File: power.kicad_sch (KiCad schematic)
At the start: 14 parts, among them U3 TPS7A2050PDQNR, U4 TPS61040DBV

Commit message: rough blocking out the pcb
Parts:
- added TP2, TP3: TestPoint, TestPoint:TestPoint_THTPad_1.5x1.5mm_Drill0.7mm, symbol Connector:TestPoint
- JP3: footprint (none) -> Jumper:SolderJumper-2_P1.3mm_Open_TrianglePad1.0x1.5mm
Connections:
- net VBOOST: now also TP2.1
- net VHAPPY: now also TP3.1
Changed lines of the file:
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@@
+	)
+	(junction
+		(at 139.7 50.8)
+		(diameter 0)
+		(color 0 0 0 0)
 	)
 	(junction
@@
 	(wire
 		(pts
-			(xy 134.62 50.8) (xy 146.05 50.8)
+			(xy 134.62 50.8) (xy 139.7 50.8)
 		)
 		(stroke
@@
 		(pts
 			(xy 97.79 60.96) (xy 91.44 60.96)
+		)
+		(stroke
+			(width 0)
+			(type default)
+		)
+	)
+	(wire
+		(pts
+			(xy 139.7 50.8) (xy 146.05 50.8)
 		)
 		(stroke
@@
 			)
 		)
-		(property "Footprint" ""
+		(property "Footprint" "Jumper:SolderJumper-2_P1.3mm_Open_TrianglePad1.0x1.5mm"
 			(at 114.3 165.1 0)
 			(effects
@@
 	)
 	(symbol
+		(lib_id "Connector:TestPoint")
+		(at 139.7 50.8 0)
+		(unit 1)
+		(exclude_from_sim no)
+		(in_bom yes)
+		(on_board yes)
+		(dnp no)
+		(fields_autoplaced yes)
+		(property "Reference" "TP2"
+			(at 142.24 46.2279 0)
+			(effects
+				(font
+					(size 1.27 1.27)
+				)
+				(justify left)
+			)
+		)
+		(property "Value" "TestPoint"
+			(at 142.24 48.7679 0)
+			(effects
+				(font
+					(size 1.27 1.27)
+				)
+				(justify left)
+			)
+		)
+		(property "Footprint" "TestPoint:TestPoint_THTPad_1.5x1.5mm_Drill0.7mm"
+			(at 144.78 50.8 0)
+			(effects
+				(font
+					(size 1.27 1.27)
+				)
+				(hide yes)
+			)
+		)
+		(property "Datasheet" "~"
+			(at 144.78 50.8 0)
+			(effects
+				(font
+					(size 1.27 1.27)
+				)
+				(hide yes)
+			)
+		)
+		(property "Description" "test point"
+			(at 139.7 50.8 0)
+			(effects
+				(font
+					(size 1.27 1.27)
+				)
+				(hide yes)
+			)
+		)
+		(pin "1"
+		)
+		(instances
+			(project ""
+				(path "/e63e39d7-6ac0-4ffd-8aa3-1841a4541b55/fdbfdc15-850a-4ffd-858c-b9b4d340c2f9"
+					(reference "TP2")
+					(unit 1)
+				)
+			)
+		)
+	)
+	(symbol
 		(lib_id "Regulator_Switching:TPS61040DBV")
 		(at 105.41 63.5 0)
@@
 					(unit 1)
 				)
+			)
+		)
+	)
+	(symbol
+		(lib_id "Connector:TestPoint")
+		(at 139.7 101.6 0)
+		(unit 1)
+		(exclude_from_sim no)
+		(in_bom yes)
+		(on_board yes)
+		(dnp no)
+		(fields_autoplaced yes)
+		(property "Reference" "TP3"
+			(at 142.24 97.0279 0)
+			(effects
+				(font
+					(size 1.27 1.27)
+				)
+				(justify left)
+			)
+		)
+		(property "Value" "TestPoint"
+			(at 142.24 99.5679 0)
+			(effects
+				(font
+					(size 1.27 1.27)
+				)
+				(justify left)
+			)
+		)
+		(property "Footprint" "TestPoint:TestPoint_THTPad_1.5x1.5mm_Drill0.7mm"
+			(at 144.78 101.6 0)
+			(effects
+				(font
+					(size 1.27 1.27)
+				)
+				(hide yes)
+			)
+		)
+		(property "Datasheet" "~"
+			(at 144.78 101.6 0)
+			(effects
+				(font
+					(size 1.27 1.27)
+				)
+				(hide yes)
+			)
+		)
+		(property "Description" "test point"
+			(at 139.7 101.6 0)
+			(effects
+				(font
+					(size 1.27 1.27)
+				)
+				(hide yes)
+			)
+		)
+		(pin "1"
+		)
+		(instances
+			(project "pi-hat-hx711_r1"
+				(path "/e63e39d7-6ac0-4ffd-8aa3-1841a4541b55/fdbfdc15-850a-4ffd-858c-b9b4d340c2f9"
+					(reference "TP3")
+					(unit 1)
+				)

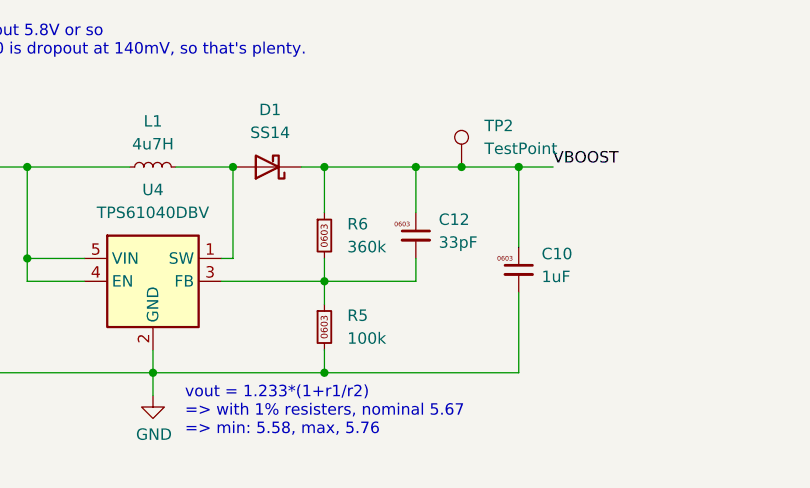
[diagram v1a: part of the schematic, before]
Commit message: better parts, start pushing layout blocks
SMA is dumb, way too big
the swpa3030 was... unnecessarily small. we're trying to be super chill
power here, don't push it hot.  (Still, 1A was.. really, more than
enough? but 1A is a 40C rise, so.. let's just have less....)
use more caps too. why the fuck not. more filtering, more happy.

holy fuck though, kicad on wayland is giving me the shits!
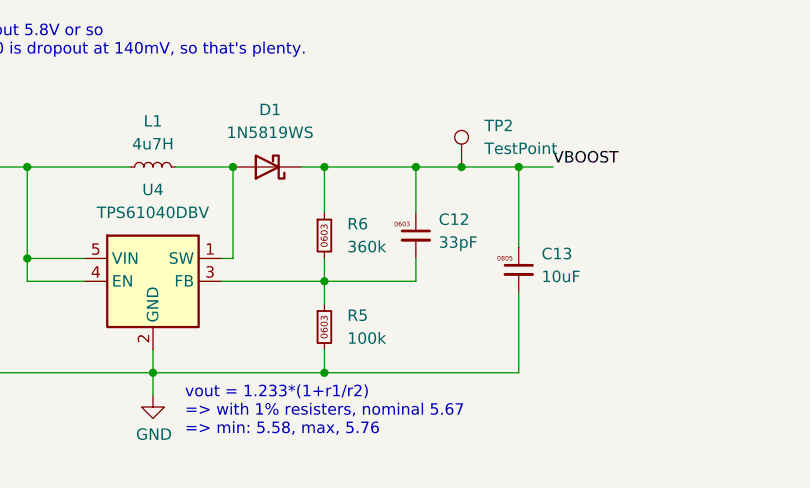
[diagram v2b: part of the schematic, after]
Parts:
- removed C10: 1uF, Capacitor_SMD:C_0603_1608Metric, symbol karl-marel-atomics:KC0603_1uF
- removed D1: SS14, Diode_SMD:D_SMA, symbol Diode:SS14
- added C13: 10uF, Capacitor_SMD:C_0805_2012Metric, symbol karl-marel-atomics:KC0805_10uF_25V
- added D1: 1N5819WS, Diode_SMD:D_SOD-323, symbol Diode:1N5819WS
- C11, C12, C6, C7, C8, R5, R6, R7: jlcbasic (none) -> basic
- L1: footprint Inductor_SMD:L_Sunlord_SWPA3015S -> Inductor_SMD:L_Changjiang_FNR4030S; LCSC Part # C19398 -> C167874; MPN SWPA3015S4R7MT -> FNR4030S4R7MT; jlcbasic (none) -> 0
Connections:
- net GND: now also C13.2
- net VBOOST: now also C13.1, D1.1 (K)
- net at L1.2, U4.1 (SW): now also D1.2 (A)

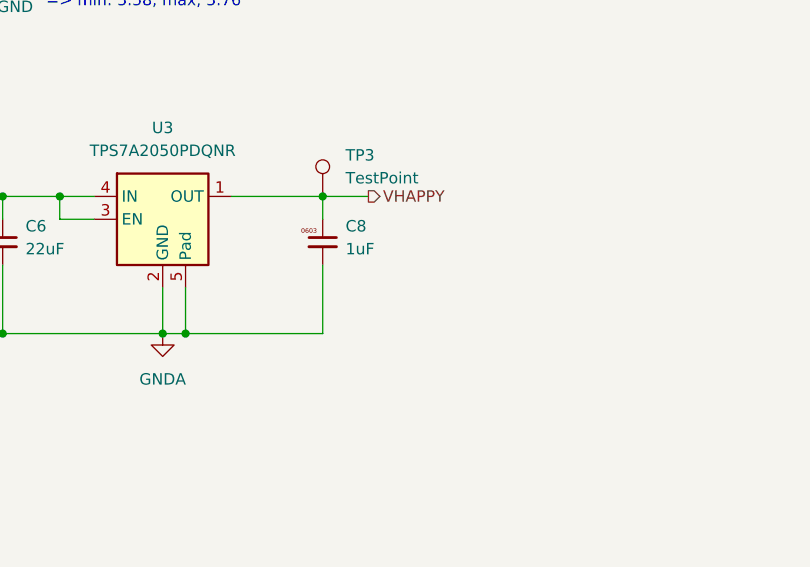
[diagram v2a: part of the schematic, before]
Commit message: add second channel input
switch to vertical connectors, so no concerns abotu edge space.
Allows offering the second channel, even though it's probably useless,
but it sets us up with a style we might be ok with for subsequent
boards.
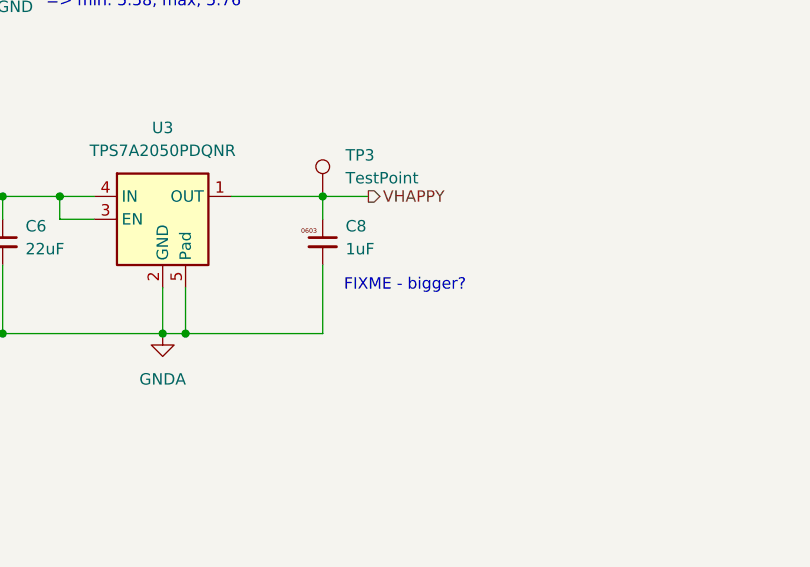
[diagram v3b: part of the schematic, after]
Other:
- note added: "FIXME - bigger?"
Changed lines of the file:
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@@
+		)
+	)
+	(text "FIXME - bigger?"
+		(exclude_from_sim no)
+		(at 148.844 111.506 0)
+		(effects
+			(font
+				(size 1.27 1.27)
+			)
 		)
 	)

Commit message: pushing blocks
roughyl how we want it?
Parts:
- added TP4: TestPoint, TestPoint:TestPoint_THTPad_1.5x1.5mm_Drill0.7mm, symbol Connector:TestPoint
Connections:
- net GNDA: now also TP4.1
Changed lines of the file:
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@@
+	)
+	(symbol
+		(lib_id "power:GNDA")
+		(at 139.7 124.46 0)
+		(unit 1)
+		(exclude_from_sim no)
+		(in_bom yes)
+		(on_board yes)
+		(dnp no)
+		(fields_autoplaced yes)
+		(property "Reference" "#PWR05"
+			(at 139.7 130.81 0)
+			(effects
+				(font
+					(size 1.27 1.27)
+				)
+				(hide yes)
+			)
+		)
+		(property "Value" "GNDA"
+			(at 139.7 129.54 0)
+			(effects
+				(font
+					(size 1.27 1.27)
+				)
+			)
+		)
+		(property "Footprint" ""
+			(at 139.7 124.46 0)
+			(effects
+				(font
+					(size 1.27 1.27)
+				)
+				(hide yes)
+			)
+		)
+		(property "Datasheet" ""
+			(at 139.7 124.46 0)
+			(effects
+				(font
+					(size 1.27 1.27)
+				)
+				(hide yes)
+			)
+		)
+		(property "Description" "Power symbol creates a global label with name \"GNDA\" , analog ground"
+			(at 139.7 124.46 0)
+			(effects
+				(font
+					(size 1.27 1.27)
+				)
+				(hide yes)
+			)
+		)
+		(pin "1"
+		)
+		(instances
+			(project "pi-hat-hx711_r1"
+				(path "/e63e39d7-6ac0-4ffd-8aa3-1841a4541b55/fdbfdc15-850a-4ffd-858c-b9b4d340c2f9"
+					(reference "#PWR05")
+					(unit 1)
+				)
+			)
+		)
 	)
 	(symbol
@@
 					(unit 1)
 				)
+			)
+		)
+	)
+	(symbol
+		(lib_id "Connector:TestPoint")
+		(at 139.7 124.46 0)
+		(unit 1)
+		(exclude_from_sim no)
+		(in_bom yes)
+		(on_board yes)
+		(dnp no)
+		(fields_autoplaced yes)
+		(property "Reference" "TP4"
+			(at 142.24 119.8879 0)
+			(effects
+				(font
+					(size 1.27 1.27)
+				)
+				(justify left)
+			)
+		)
+		(property "Value" "TestPoint"
+			(at 142.24 122.4279 0)
+			(effects
+				(font
+					(size 1.27 1.27)
+				)
+				(justify left)
+			)
+		)
+		(property "Footprint" "TestPoint:TestPoint_THTPad_1.5x1.5mm_Drill0.7mm"
+			(at 144.78 124.46 0)
+			(effects
+				(font
+					(size 1.27 1.27)
+				)
+				(hide yes)
+			)
+		)
+		(property "Datasheet" "~"
+			(at 144.78 124.46 0)
+			(effects
+				(font
+					(size 1.27 1.27)
+				)
+				(hide yes)
+			)
+		)
+		(property "Description" "test point"
+			(at 139.7 124.46 0)
+			(effects
+				(font
+					(size 1.27 1.27)
+				)
+				(hide yes)
+			)
+		)
+		(pin "1"
+		)
+		(instances
+			(project "pi-hat-hx711_r1"
+				(path "/e63e39d7-6ac0-4ffd-8aa3-1841a4541b55/fdbfdc15-850a-4ffd-858c-b9b4d340c2f9"
+					(reference "TP4")
+					(unit 1)
+				)

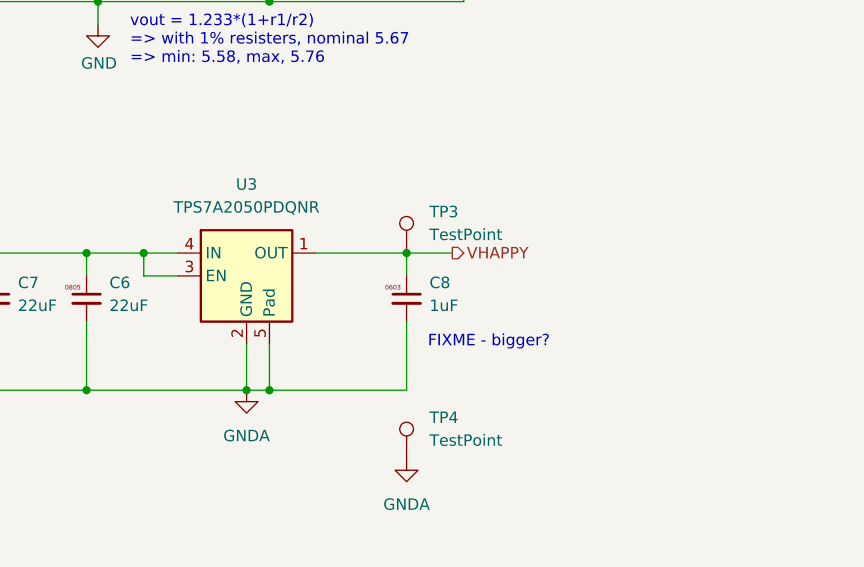
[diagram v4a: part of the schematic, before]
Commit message: chunk out routing
looks okish?

switched x2son for plain sot235, it's better stocked at jlc anyway, and
easier to probe and work with.
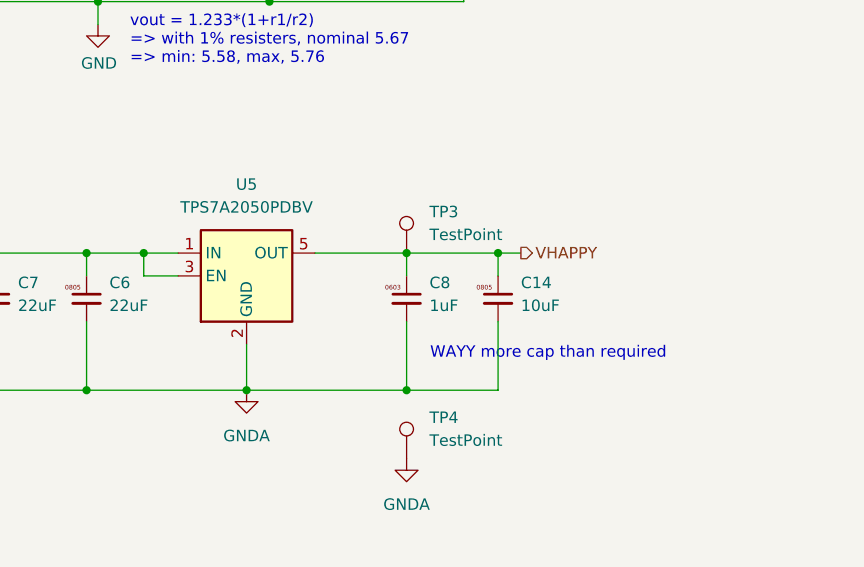
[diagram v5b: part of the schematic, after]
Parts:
- removed U3: TPS7A2050PDQNR, Package_SON:Texas_X2SON-4_1x1mm_P0.65mm, symbol Regulator_Linear:TPS7A20xxxDQN
- added C14: 10uF, Capacitor_SMD:C_0805_2012Metric, symbol karl-marel-atomics:KC0805_10uF_25V
- added U5: TPS7A2050PDBV, Package_TO_SOT_SMD:SOT-23-5, symbol Regulator_Linear:TPS7A0515PDBV
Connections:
- net GNDA: now also C14.2, U5.2 (GND)
- net VHAPPY: now also C14.1, U5.5 (OUT)
- net at C6.1, C7.1, R7.2: now also U5.1 (IN), U5.3 (EN)
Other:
- note added: "WAYY more cap than required"
- note removed: "FIXME - bigger?"
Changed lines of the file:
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@@
-		)
-	)
-	(text "FIXME - bigger?"
-		(exclude_from_sim no)
-		(at 148.844 111.506 0)
-		(effects
-			(font
-				(size 1.27 1.27)
-			)
 		)
 	)
@@
 		)
 	)
-	(junction
-		(at 124.46 116.84)
-		(diameter 0)
-		(color 0 0 0 0)
+	(text "WAYY more cap than required"
+		(exclude_from_sim no)
+		(at 155.448 112.776 0)
+		(effects
+			(font
+				(size 1.27 1.27)
+			)
+		)
 	)
 	(junction
@@
 	)
 	(junction
+		(at 149.86 101.6)
+		(diameter 0)
+		(color 0 0 0 0)
+	)
+	(junction
 		(at 80.01 50.8)
 		(diameter 0)
@@
 	)
 	(junction
+		(at 139.7 116.84)
+		(diameter 0)
+		(color 0 0 0 0)
+	)
+	(junction
 		(at 146.05 50.8)
 		(diameter 0)
@@
 	(wire
 		(pts
-			(xy 124.46 111.76) (xy 124.46 116.84)
-		)
-		(stroke
-			(width 0)
-			(type default)
-		)
-	)
-	(wire
-		(pts
 			(xy 76.2 50.8) (xy 80.01 50.8)
 		)
@@
 	(wire
 		(pts
+			(xy 149.86 101.6) (xy 149.86 104.14)
+		)
+		(stroke
+			(width 0)
+			(type default)
+		)
+	)
+	(wire
+		(pts
 			(xy 91.44 50.8) (xy 102.87 50.8)
 		)
@@
 	(wire
 		(pts
-			(xy 124.46 116.84) (xy 121.92 116.84)
+			(xy 121.92 116.84) (xy 139.7 116.84)
 		)
 		(stroke
@@
 	(wire
 		(pts
+			(xy 149.86 116.84) (xy 139.7 116.84)
+		)
+		(stroke
+			(width 0)
+			(type default)
+		)
+	)
+	(wire
+		(pts
 			(xy 104.14 101.6) (xy 110.49 101.6)
 		)
@@
 	(wire
 		(pts
+			(xy 149.86 109.22) (xy 149.86 116.84)
+		)
+		(stroke
+			(width 0)
+			(type default)
+		)
+	)
+	(wire
+		(pts
 			(xy 104.14 116.84) (xy 121.92 116.84)
 		)
@@
 	(wire
 		(pts
-			(xy 139.7 116.84) (xy 124.46 116.84)
-		)
-		(stroke
-			(width 0)
-			(type default)
-		)
-	)
-	(wire
-		(pts
 			(xy 93.98 101.6) (xy 93.98 104.14)
 		)
@@
 	(wire
 		(pts
-			(xy 139.7 101.6) (xy 144.78 101.6)
+			(xy 139.7 101.6) (xy 149.86 101.6)
 		)
 		(stroke
@@
 		(pts
 			(xy 124.46 60.96) (xy 124.46 63.5)
+		)
+		(stroke
+			(width 0)
+			(type default)
+		)
+	)
+	(wire
+		(pts
+			(xy 149.86 101.6) (xy 152.4 101.6)
 		)
 		(stroke
@@
 	(hierarchical_label "VHAPPY"
 		(shape output)
-		(at 144.78 101.6 0)
+		(at 152.4 101.6 0)
 		(effects
 			(font
@@
 	)
 	(symbol
+		(lib_id "karl-marel-atomics:KC0805_10uF_25V")
+		(at 149.86 106.68 0)
+		(unit 1)
+		(exclude_from_sim no)
+		(in_bom yes)
+		(on_board yes)
+		(dnp no)
+		(fields_autoplaced yes)
+		(property "Reference" "C14"
+			(at 152.4 104.9071 0)
+			(effects
+				(font
+					(size 1.27 1.27)
+				)
+				(justify left)
+			)
+		)
+		(property "Value" "10uF"
+			(at 152.4 107.4471 0)
+			(effects
+				(font
+					(size 1.27 1.27)
+				)
+				(justify left)
+			)
+		)
+		(property "Footprint" "Capacitor_SMD:C_0805_2012Metric"
+			(at 149.352 110.49 0)
+			(effects
+				(font
+					(size 1.27 1.27)
+				)
+				(hide yes)
+			)
+		)
+		(property "Datasheet" "~"
+			(at 149.86 106.68 0)
+			(effects
+				(font
+					(size 1.27 1.27)
+				)
+				(hide yes)
+			)
+		)
+		(property "Description" "25V, X5R"
+			(at 149.86 110.49 0)
+			(effects
+				(font
+					(size 1.27 1.27)
+				)
+				(hide yes)
+			)
+		)
+		(property "MPN" "CL21A106KAYNNNE"
+			(at 149.606 110.49 0)
+			(effects
+				(font
+					(size 1.27 1.27)
+				)
+				(hide yes)
+			)
+		)
+		(property "LCSC Part #" "C15850"
+			(at 149.86 110.49 0)
+			(effects
+				(font
+					(size 1.27 1.27)
+				)
+				(hide yes)
+			)
+		)
+		(property "jlcbasic" "basic"
+			(at 149.86 106.68 0)
+			(effects
+				(font
+					(size 1.27 1.27)
+				)
+				(hide yes)
+			)
+		)
+		(pin "1"
+		)
+		(pin "2"
+		)
+		(instances
+			(project "pi-hat-hx711_r1"
+				(path "/e63e39d7-6ac0-4ffd-8aa3-1841a4541b55/fdbfdc15-850a-4ffd-858c-b9b4d340c2f9"
+					(reference "C14")
+					(unit 1)
+				)
+			)
+		)
+	)
+	(symbol
 		(lib_id "karl-marel-atomics:KC0805_22uF_25V")
 		(at 80.01 60.96 0)
@@
 	)
 	(symbol
-		(lib_id "Regulator_Linear:TPS7A20xxxDQN")
-		(at 121.92 104.14 0)
-		(unit 1)
-		(exclude_from_sim no)
-		(in_bom yes)
-		(on_board yes)
-		(dnp no)
-		(fields_autoplaced yes)
-		(property "Reference" "U3"
-			(at 121.92 93.98 0)
-			(effects
-				(font
-					(size 1.27 1.27)
-				)
-			)
-		)
-		(property "Value" "TPS7A2050PDQNR"
-			(at 121.92 96.52 0)
-			(effects
-				(font
-					(size 1.27 1.27)
-				)
-			)
-		)
-		(property "Footprint" "Package_SON:Texas_X2SON-4_1x1mm_P0.65mm"
-			(at 121.92 95.25 0)
-			(effects
-				(font
-					(size 1.27 1.27)
-				)
-				(hide yes)
-			)
-		)
-		(property "Datasheet" "https://www.ti.com/lit/ds/symlink/tps7a20.pdf"
-			(at 121.92 91.44 0)
-			(effects
-				(font
-					(size 1.27 1.27)
-				)
-				(hide yes)
-			)
-		)
-		(property "Description" "300 mA Low Dropout Voltage Regulator, Fixed Output, 1.6..6.0Vin, Low-Noise (7μV RMS), 6.5μA IQ LDO, X2SON-5"
-			(at 121.92 104.14 0)
-			(effects
-				(font
-					(size 1.27 1.27)
-				)
-				(hide yes)
-			)
-		)
-		(property "LCSC Part #" "C2866499"
-			(at 121.92 104.14 0)
-			(effects
-				(font
-					(size 1.27 1.27)
-				)
-				(hide yes)
-			)
-		)
-		(property "MPN" "TPS7A2050PDQNR"
-			(at 121.92 104.14 0)
-			(effects
-				(font
-					(size 1.27 1.27)
-				)
-				(hide yes)
-			)
-		)
-		(property "jlcbasic" "0"
-			(at 121.92 104.14 0)
-			(effects
-				(font
-					(size 1.27 1.27)
-				)
-				(hide yes)
-			)
-		)
-		(pin "1"
-		)
-		(pin "5"
-		)
-		(pin "4"
-		)
-		(pin "3"
-		)
-		(pin "2"
-		)
-		(instances
-			(project "pi-hat-hx711_r1"
-				(path "/e63e39d7-6ac0-4ffd-8aa3-1841a4541b55/fdbfdc15-850a-4ffd-858c-b9b4d340c2f9"
-					(reference "U3")
-					(unit 1)
-				)
-			)
-		)
-	)
-	(symbol
 		(lib_id "Diode:1N5819WS")
 		(at 118.11 50.8 180)
@@
 					(unit 1)
 				)
+			)
+		)
+	)
+	(symbol
+		(lib_id "Regulator_Linear:TPS7A0515PDBV")
+		(at 121.92 104.14 0)
+		(unit 1)
+		(exclude_from_sim no)
+		(in_bom yes)
+		(on_board yes)
+		(dnp no)
+		(fields_autoplaced yes)
+		(property "Reference" "U5"
+			(at 121.92 93.98 0)
+			(effects
+				(font
+					(size 1.27 1.27)
+				)
+			)
+		)
+		(property "Value" "TPS7A2050PDBV"
+			(at 121.92 96.52 0)
+			(effects
+				(font
+					(size 1.27 1.27)
+				)
+			)
+		)
+		(property "Footprint" "Package_TO_SOT_SMD:SOT-23-5"
+			(at 121.92 95.25 0)
+			(effects
+				(font
+					(size 1.27 1.27)
+				)
+				(hide yes)
+			)
+		)
+		(property "Datasheet" "https://www.ti.com/lit/ds/symlink/tps7a20.pdf"
+			(at 121.92 91.44 0)
+			(effects
+				(font
+					(size 1.27 1.27)
+				)
+				(hide yes)
+			)
+		)
+		(property "Description" "300 mA Low Dropout Voltage Regulator, Fixed Output, 1.6..6.0Vin, Low-Noise (7μV RMS), 6.5μA IQ LDO, SOT-23-5"
+			(at 121.92 104.14 0)
+			(effects
+				(font
+					(size 1.27 1.27)
+				)
+				(hide yes)
+			)
+		)
+		(property "LCSC Part #" "C2864504"
+			(at 121.92 104.14 0)
+			(effects
+				(font
+					(size 1.27 1.27)
+				)
+				(hide yes)
+			)
+		)
+		(property "MPN" "TPS7A2050PDBVR"
+			(at 121.92 104.14 0)
+			(effects
+				(font
+					(size 1.27 1.27)
+				)
+				(hide yes)
+			)
+		)
+		(property "jlcbasic" "0"
+			(at 121.92 104.14 0)
+			(effects
+				(font
+					(size 1.27 1.27)
+				)
+				(hide yes)
+			)
+		)
+		(pin "4"
+		)
+		(pin "2"
+		)
+		(pin "5"
+		)
+		(pin "3"
+		)
+		(pin "1"
+		)
+		(instances
+			(project ""
+				(path "/e63e39d7-6ac0-4ffd-8aa3-1841a4541b55/fdbfdc15-850a-4ffd-858c-b9b4d340c2f9"
+					(reference "U5")
+					(unit 1)
+				)

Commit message: pushing silk, are we done?!
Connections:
- net VBOOST_F: now reaches C6.1, C7.1, R7.2, U5.1 (IN), U5.3 (EN)
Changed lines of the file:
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@@
+		)
+	)
+	(label "VBOOST_F"
+		(at 105.41 101.6 180)
+		(effects
+			(font
+				(size 1.27 1.27)
+			)
+			(justify right bottom)
 		)
 	)

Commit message: wheeww!
Added 3.3v supply from 5V by default.
Added header to access IOs without rpi
Added TP to supply/monitor raw 5V (use without pi)
Adjusted TPs to be on 2.54mm spacing to get headers if desired
Added TVS on EXE+ lines.
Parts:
- TP2, TP3, TP4: footprint TestPoint:TestPoint_THTPad_1.5x1.5mm_Drill0.7mm -> TestPoint:TestPoint_THTPad_2.0x2.0mm_Drill1.0mm
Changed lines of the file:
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@@
 			)
 		)
-		(property "Footprint" "TestPoint:TestPoint_THTPad_1.5x1.5mm_Drill0.7mm"
+		(property "Footprint" "TestPoint:TestPoint_THTPad_2.0x2.0mm_Drill1.0mm"
 			(at 144.78 50.8 0)
 			(effects
@@
 			)
 		)
-		(property "Footprint" "TestPoint:TestPoint_THTPad_1.5x1.5mm_Drill0.7mm"
+		(property "Footprint" "TestPoint:TestPoint_THTPad_2.0x2.0mm_Drill1.0mm"
 			(at 144.78 101.6 0)
 			(effects
@@
 			)
 		)
-		(property "Footprint" "TestPoint:TestPoint_THTPad_1.5x1.5mm_Drill0.7mm"
+		(property "Footprint" "TestPoint:TestPoint_THTPad_2.0x2.0mm_Drill1.0mm"
 			(at 144.78 124.46 0)
 			(effects
